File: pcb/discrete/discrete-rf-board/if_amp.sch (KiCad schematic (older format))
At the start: 48 parts

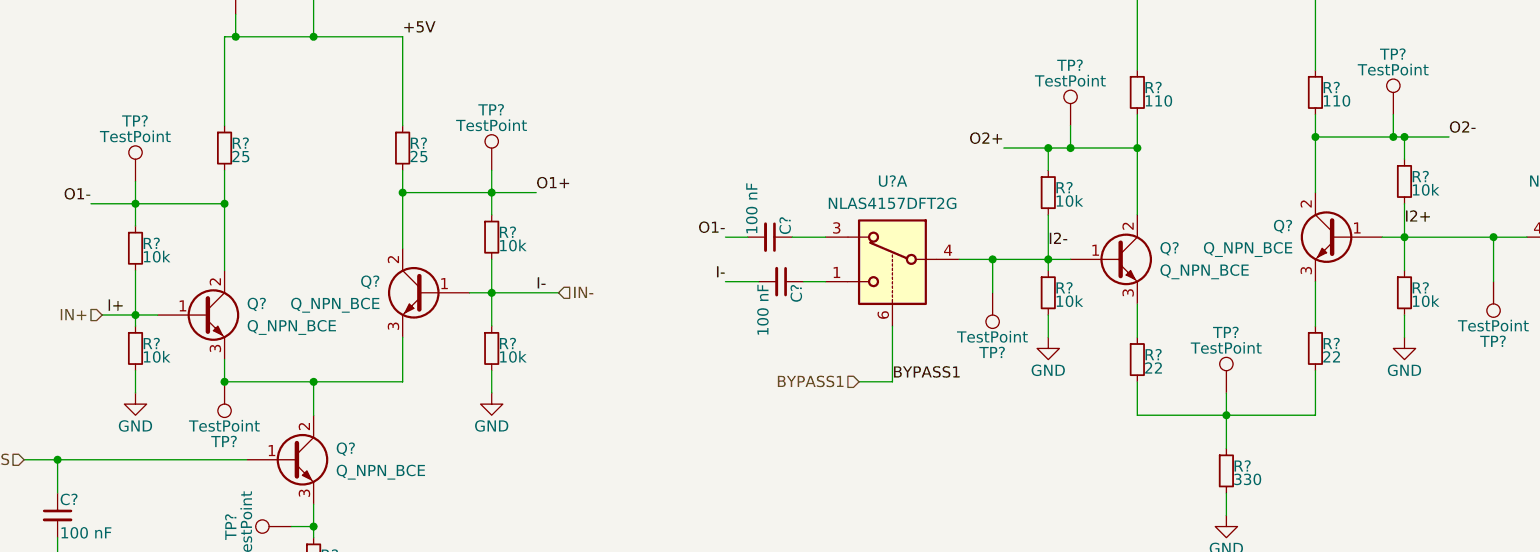
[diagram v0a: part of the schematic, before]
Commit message: Picked matched NPNs for IF amplifier stages
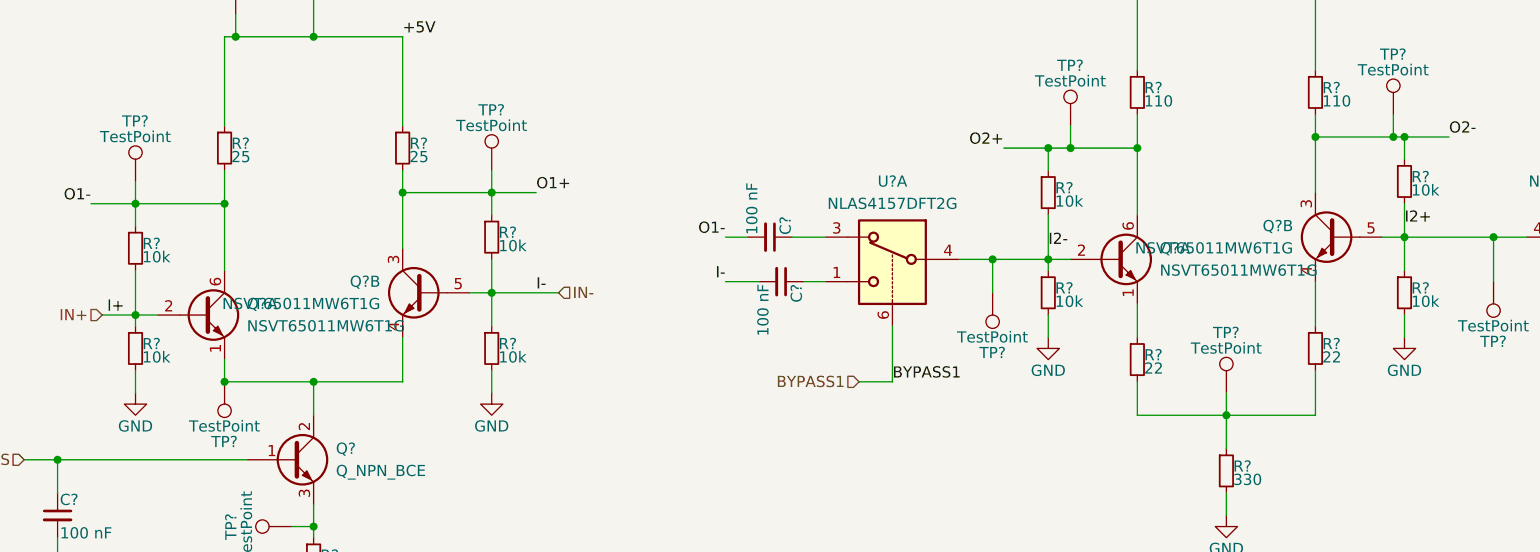
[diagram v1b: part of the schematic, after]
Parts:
- removed Q? (x4): Q_NPN_BCE, symbol Device:Q_NPN_BCE
- added Q? (x4): NSVT65011MW6T1G, symbol Device:Q_DUAL_NPN_NPN_E1B1C2E2B2C1
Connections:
- net I2+: now also Q?.5 (B2)
- net I2-: now also Q?.2 (B1)
- net IN+: now also Q?.2 (B1)
- net IN-: now also Q?.5 (B2)
- net O1+: now also Q?.3 (C2)
- net O1-: now also Q?.6 (C1)
- net O2+: now also Q?.6 (C1)
- net O2-: now also Q?.3 (C2)
- net at Q?.2 (C), TP?.1: now also Q?.1 (E1), Q?.4 (E2)
- net at R?.1: now also Q?.1 (E1)
- net at R?.1: now also Q?.4 (E2)
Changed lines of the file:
@@
 $EndDescr
-$Comp
-L Device:Q_NPN_BCE Q?
-U 1 1 5CC4E7E9
-P 1950 3000
-F 0 "Q?" H 2150 3050 50  0000 L CNN
-F 1 "Q_NPN_BCE" H 2150 2950 50  0000 L CNN
-F 2 "" H 2150 3100 50  0001 C CNN
-F 3 "~" H 1950 3000 50  0001 C CNN
-	1    1950 3000
-	1    0    0    -1
-$EndComp
-$Comp
-L Device:Q_NPN_BCE Q?
-U 1 1 5CC4EAD4
-P 2950 2900
-F 0 "Q?" H 3150 2950 50  0000 L CNN
-F 1 "Q_NPN_BCE" H 3150 2850 50  0000 L CNN
-F 2 "" H 3150 3000 50  0001 C CNN
-F 3 "~" H 2950 2900 50  0001 C CNN
-	1    2950 2900
-	-1   0    0    -1
-$EndComp
 $Comp
 L Device:R_Small R?
@@
 Wire Wire Line
 	1300 4000 1300 4150
-$Comp
-L Device:Q_NPN_BCE Q?
-U 1 1 5CC71002
-P 6050 2750
-F 0 "Q?" H 6250 2800 50  0000 L CNN
-F 1 "Q_NPN_BCE" H 6250 2700 50  0000 L CNN
-F 2 "" H 6250 2850 50  0001 C CNN
-F 3 "~" H 6050 2750 50  0001 C CNN
-	1    6050 2750
-	1    0    0    -1
-$EndComp
-$Comp
-L Device:Q_NPN_BCE Q?
-U 1 1 5CC71008
-P 7050 2650
-F 0 "Q?" H 7250 2700 50  0000 L CNN
-F 1 "Q_NPN_BCE" H 7250 2600 50  0000 L CNN
-F 2 "" H 7250 2750 50  0001 C CNN
-F 3 "~" H 7050 2650 50  0001 C CNN
-	1    7050 2650
-	-1   0    0    -1
-$EndComp
 $Comp
 L Device:R_Small R?
@@
 Wire Wire Line
 	6550 3350 6550 3450
+$Comp
+L Device:Q_DUAL_NPN_NPN_E1B1C2E2B2C1 Q?
+U 1 1 5CC8B3B3
+P 1950 3000
+F 0 "Q?" H 2150 3050 50  0000 L CNN
+F 1 "NSVT65011MW6T1G" H 2150 2950 50  0000 L CNN
+F 2 "" H 2150 3100 50  0001 C CNN
+F 3 "~" H 1950 3000 50  0001 C CNN
+	1    1950 3000
+	1    0    0    -1
+$EndComp
+$Comp
+L Device:Q_DUAL_NPN_NPN_E1B1C2E2B2C1 Q?
+U 2 1 5CC8BBB5
+P 2950 2900
+F 0 "Q?" H 3150 2950 50  0000 L CNN
+F 1 "NSVT65011MW6T1G" H 3150 2850 50  0000 L CNN
+F 2 "" H 3150 3000 50  0001 C CNN
+F 3 "~" H 2950 2900 50  0001 C CNN
+	2    2950 2900
+	-1   0    0    -1
+$EndComp
+$Comp
+L Device:Q_DUAL_NPN_NPN_E1B1C2E2B2C1 Q?
+U 1 1 5CC8C47F
+P 6050 2750
+F 0 "Q?" H 6250 2800 50  0000 L CNN
+F 1 "NSVT65011MW6T1G" H 6250 2700 50  0000 L CNN
+F 2 "" H 6250 2850 50  0001 C CNN
+F 3 "~" H 6050 2750 50  0001 C CNN
+	1    6050 2750
+	1    0    0    -1
+$EndComp
+$Comp
+L Device:Q_DUAL_NPN_NPN_E1B1C2E2B2C1 Q?
+U 2 1 5CC8CC50
+P 7050 2650
+F 0 "Q?" H 7250 2700 50  0000 L CNN
+F 1 "NSVT65011MW6T1G" H 7250 2600 50  0000 L CNN
+F 2 "" H 7250 2750 50  0001 C CNN
+F 3 "~" H 7050 2650 50  0001 C CNN
+	2    7050 2650
+	-1   0    0    -1
+$EndComp
 $EndSCHEMATC

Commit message: Save changes while moving over to the new laptop
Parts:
- gave numbers to parts that had none: 42

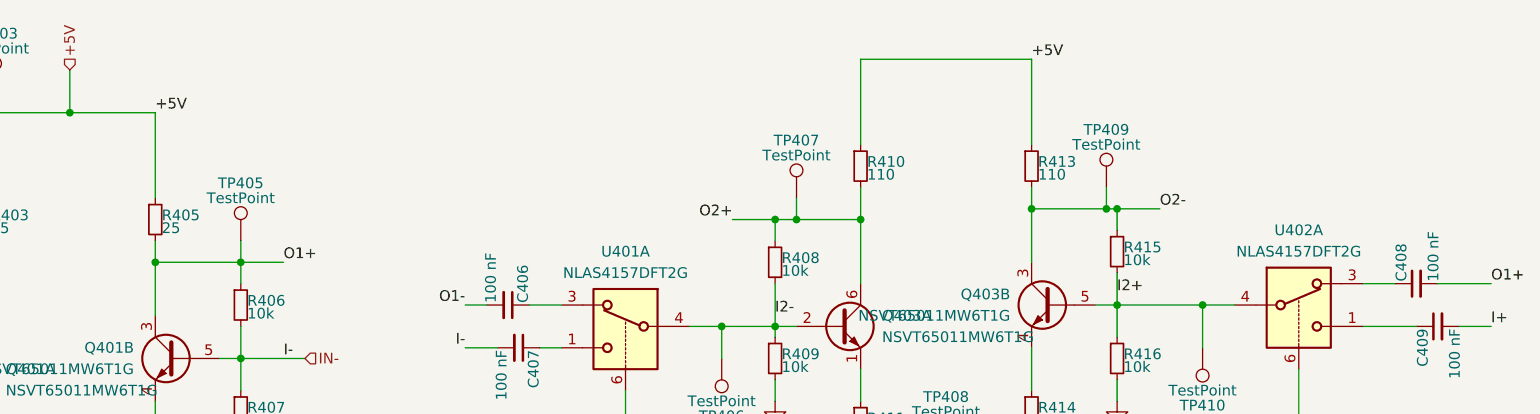
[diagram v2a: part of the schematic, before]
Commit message: Work on LNA staging, attenuator design, various fixes elsewhere
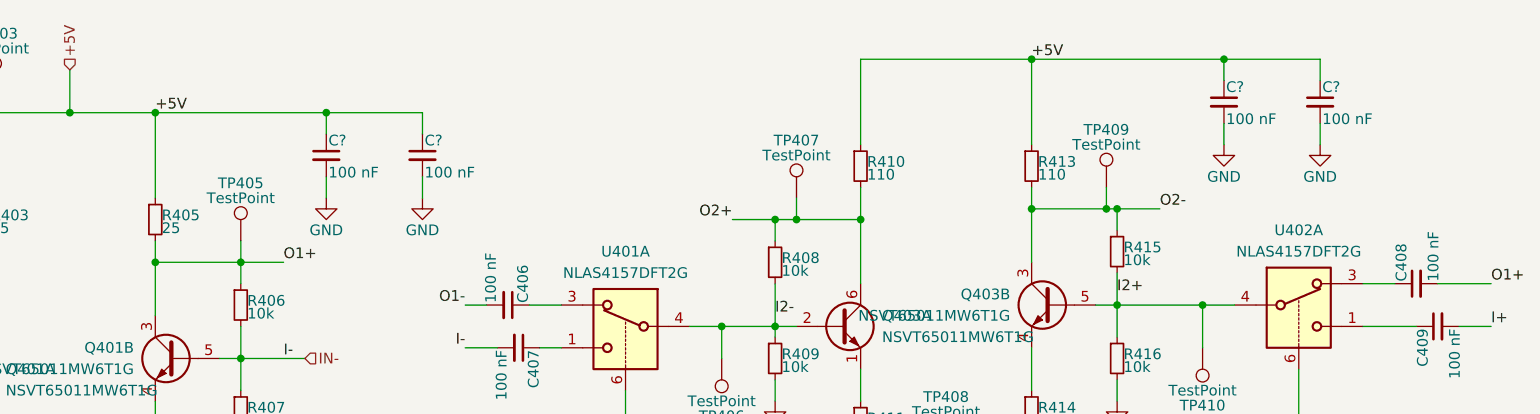
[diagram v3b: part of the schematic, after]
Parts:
- added C? (x4): 100 nF, symbol Device:C_Small
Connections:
- net +5V: now also C?.1, C?.1, C?.1, C?.1
- net GND: now also C?.2, C?.2, C?.2, C?.2
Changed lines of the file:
@@
 $Descr A4 11693 8268
 encoding utf-8
-Sheet 4 11
+Sheet 4 16
 Title ""
 Date ""
@@
 	-1   0    0    -1
 $EndComp
+$Comp
+L Device:C_Small C?
+U 1 1 5D57AB5D
+P 3650 1950
+AR Path="/5CA6B0AA/5CC4DFC2/5D57AB5D" Ref="C?"  Part="1"
+AR Path="/5CA6B0AA/5CC9409A/5D57AB5D" Ref="C?"  Part="1"
+F 0 "C?" H 3660 2020 50  0000 L CNN
+F 1 "100 nF" H 3660 1870 50  0000 L CNN
+F 2 "" H 3650 1950 50  0001 C CNN
+F 3 "~" H 3650 1950 50  0001 C CNN
+	1    3650 1950
+	1    0    0    -1
+$EndComp
+$Comp
+L Device:C_Small C?
+U 1 1 5D57AB63
+P 4100 1950
+AR Path="/5CA6B0AA/5CC4DFC2/5D57AB63" Ref="C?"  Part="1"
+AR Path="/5CA6B0AA/5CC9409A/5D57AB63" Ref="C?"  Part="1"
+F 0 "C?" H 4110 2020 50  0000 L CNN
+F 1 "100 nF" H 4110 1870 50  0000 L CNN
+F 2 "" H 4100 1950 50  0001 C CNN
+F 3 "~" H 4100 1950 50  0001 C CNN
+	1    4100 1950
+	1    0    0    -1
+$EndComp
+$Comp
+L power:GND #PWR?
+U 1 1 5D57AB69
+P 3650 2150
+AR Path="/5CA6B0AA/5CC4DFC2/5D57AB69" Ref="#PWR?"  Part="1"
+AR Path="/5CA6B0AA/5CC9409A/5D57AB69" Ref="#PWR?"  Part="1"
+F 0 "#PWR?" H 3650 1900 50  0001 C CNN
+F 1 "GND" H 3650 2000 50  0000 C CNN
+F 2 "" H 3650 2150 50  0001 C CNN
+F 3 "" H 3650 2150 50  0001 C CNN
+	1    3650 2150
+	1    0    0    -1
+$EndComp
+$Comp
+L power:GND #PWR?
+U 1 1 5D57AB6F
+P 4100 2150
+AR Path="/5CA6B0AA/5CC4DFC2/5D57AB6F" Ref="#PWR?"  Part="1"
+AR Path="/5CA6B0AA/5CC9409A/5D57AB6F" Ref="#PWR?"  Part="1"
+F 0 "#PWR?" H 4100 1900 50  0001 C CNN
+F 1 "GND" H 4100 2000 50  0000 C CNN
+F 2 "" H 4100 2150 50  0001 C CNN
+F 3 "" H 4100 2150 50  0001 C CNN
+	1    4100 2150
+	1    0    0    -1
+$EndComp
+Wire Wire Line
+	4100 2150 4100 2050
+Wire Wire Line
+	3650 2050 3650 2150
+Wire Wire Line
+	4100 1750 4100 1850
+Wire Wire Line
+	3650 1850 3650 1750
+Connection ~ 3650 1750
+Wire Wire Line
+	3650 1750 4100 1750
+$Comp
+L Device:C_Small C?
+U 1 1 5D580ACE
+P 7850 1700
+AR Path="/5CA6B0AA/5CC4DFC2/5D580ACE" Ref="C?"  Part="1"
+AR Path="/5CA6B0AA/5CC9409A/5D580ACE" Ref="C?"  Part="1"
+F 0 "C?" H 7860 1770 50  0000 L CNN
+F 1 "100 nF" H 7860 1620 50  0000 L CNN
+F 2 "" H 7850 1700 50  0001 C CNN
+F 3 "~" H 7850 1700 50  0001 C CNN
+	1    7850 1700
+	1    0    0    -1
+$EndComp
+$Comp
+L Device:C_Small C?
+U 1 1 5D580AD4
+P 8300 1700
+AR Path="/5CA6B0AA/5CC4DFC2/5D580AD4" Ref="C?"  Part="1"
+AR Path="/5CA6B0AA/5CC9409A/5D580AD4" Ref="C?"  Part="1"
+F 0 "C?" H 8310 1770 50  0000 L CNN
+F 1 "100 nF" H 8310 1620 50  0000 L CNN
+F 2 "" H 8300 1700 50  0001 C CNN
+F 3 "~" H 8300 1700 50  0001 C CNN
+	1    8300 1700
+	1    0    0    -1
+$EndComp
+$Comp
+L power:GND #PWR?
+U 1 1 5D580ADA
+P 7850 1900
+AR Path="/5CA6B0AA/5CC4DFC2/5D580ADA" Ref="#PWR?"  Part="1"
+AR Path="/5CA6B0AA/5CC9409A/5D580ADA" Ref="#PWR?"  Part="1"
+F 0 "#PWR?" H 7850 1650 50  0001 C CNN
+F 1 "GND" H 7850 1750 50  0000 C CNN
+F 2 "" H 7850 1900 50  0001 C CNN
+F 3 "" H 7850 1900 50  0001 C CNN
+	1    7850 1900
+	1    0    0    -1
+$EndComp
+$Comp
+L power:GND #PWR?
+U 1 1 5D580AE0
+P 8300 1900
+AR Path="/5CA6B0AA/5CC4DFC2/5D580AE0" Ref="#PWR?"  Part="1"
+AR Path="/5CA6B0AA/5CC9409A/5D580AE0" Ref="#PWR?"  Part="1"
+F 0 "#PWR?" H 8300 1650 50  0001 C CNN
+F 1 "GND" H 8300 1750 50  0000 C CNN
+F 2 "" H 8300 1900 50  0001 C CNN
+F 3 "" H 8300 1900 50  0001 C CNN
+	1    8300 1900
+	1    0    0    -1
+$EndComp
+Wire Wire Line
+	8300 1900 8300 1800
+Wire Wire Line
+	7850 1800 7850 1900
+Wire Wire Line
+	8300 1500 8300 1600
+Wire Wire Line
+	7850 1600 7850 1500
+Connection ~ 7850 1500
+Wire Wire Line
+	7850 1500 8300 1500
+Wire Wire Line
+	6950 1500 7850 1500
+Connection ~ 6950 1500
+Wire Wire Line
+	2850 1750 3650 1750
+Connection ~ 2850 1750
 $EndSCHEMATC

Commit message: Merge stuff I guess, hopefully this doesn't break too much
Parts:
- gave numbers to parts that had none: 4
- renumbered C404 to C405, C405 to C407, C406 to C408, C407 to C409, C408 to C412, C409 to C413
